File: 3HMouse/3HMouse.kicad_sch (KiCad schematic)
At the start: 78 parts, among them J1 USB_C_Receptacle, SW1 CherryMX, SW10 CherryMX, SW11 CherryMX, SW12 CherryMX, SW13 CherryMX, SW14 CherryMX, SW15 CherryMX, SW16 CherryMX, SW17 CherryMX, SW18 CherryMX, SW19 CherryMX, SW2 CherryMX, SW20 CherryMX, SW21 CherryMX, SW22 CherryMX, SW23 CherryMX, SW24 CherryMX, SW25 CherryMX, SW26 RotaryEncoder, SW27 RotaryEncoder, SW28 CherryMX, SW29 CherryMX, SW3 CherryMX, SW30 CherryMX, SW31 CherryMX, SW32 SW_Push, SW4 CherryMX, SW5 CherryMX, SW6 CherryMX, SW7 CherryMX, SW8 CherryMX, SW9 CherryMX, U1 AT90USB1286-A, Y1 16 MHz

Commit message: Updated Numbering for switches
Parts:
- renumbered SW28 to SW26, SW29 to SW27, SW30 to SW28, SW31 to SW29, SW26 to SW30, SW27 to SW31
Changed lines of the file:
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@@
   )
   (symbol (lib_id "CherryMX:CherryMX") (at 157.48 95.885 0) (unit 1)
-    (in_bom yes) (on_board yes) (fields_autoplaced)
-    (property "Reference" "SW31" (id 0) (at 157.48 88.265 0))
+    (in_bom yes) (on_board yes)
+    (property "Reference" "SW29" (id 0) (at 157.48 88.265 0))
     (property "Value" "CherryMX" (id 1) (at 157.48 90.805 0))
     (property "Footprint" "MX_Only:MXOnly-1U" (id 2) (at 157.48 95.25 0)
@@
   )
   (symbol (lib_id "CherryMX:CherryMX") (at 143.51 95.885 0) (unit 1)
-    (in_bom yes) (on_board yes) (fields_autoplaced)
-    (property "Reference" "SW29" (id 0) (at 143.51 88.265 0))
+    (in_bom yes) (on_board yes)
+    (property "Reference" "SW27" (id 0) (at 143.51 88.265 0))
     (property "Value" "CherryMX" (id 1) (at 143.51 90.805 0))
     (property "Footprint" "MX_Only:MXOnly-1U" (id 2) (at 143.51 95.25 0)
@@
   (symbol (lib_id "Device:RotaryEncoder") (at 133.35 34.29 0) (unit 1)
     (in_bom yes) (on_board yes) (fields_autoplaced)
-    (property "Reference" "SW26" (id 0) (at 139.7 33.0199 0)
+    (property "Reference" "SW30" (id 0) (at 139.7 33.0199 0)
       (effects (font (size 1.27 1.27)) (justify left))
     )
@@
   )
   (symbol (lib_id "CherryMX:CherryMX") (at 157.48 80.645 0) (unit 1)
-    (in_bom yes) (on_board yes) (fields_autoplaced)
-    (property "Reference" "SW30" (id 0) (at 157.48 73.025 0))
+    (in_bom yes) (on_board yes)
+    (property "Reference" "SW28" (id 0) (at 157.48 73.025 0))
     (property "Value" "CherryMX" (id 1) (at 157.48 75.565 0))
     (property "Footprint" "MX_Only:MXOnly-1U" (id 2) (at 157.48 80.01 0)
@@
   (symbol (lib_id "Device:RotaryEncoder") (at 133.35 46.355 0) (unit 1)
     (in_bom yes) (on_board yes) (fields_autoplaced)
-    (property "Reference" "SW27" (id 0) (at 139.7 45.0849 0)
+    (property "Reference" "SW31" (id 0) (at 139.7 45.0849 0)
       (effects (font (size 1.27 1.27)) (justify left))
     )
@@
   )
   (symbol (lib_id "CherryMX:CherryMX") (at 143.51 80.645 0) (unit 1)
-    (in_bom yes) (on_board yes) (fields_autoplaced)
-    (property "Reference" "SW28" (id 0) (at 143.51 73.025 0))
+    (in_bom yes) (on_board yes)
+    (property "Reference" "SW26" (id 0) (at 143.51 73.025 0))
     (property "Value" "CherryMX" (id 1) (at 143.51 75.565 0))
     (property "Footprint" "MX_Only:MXOnly-1U" (id 2) (at 143.51 80.01 0)
@@
       (reference "SW25") (unit 1) (value "CherryMX") (footprint "MX_Only:MXOnly-1U")
     )
+    (path "/e0216e84-2ce2-4d70-a198-14f8e2650f46"
+      (reference "SW26") (unit 1) (value "CherryMX") (footprint "MX_Only:MXOnly-1U")
+    )
+    (path "/0fa31cb8-7672-48e3-a3df-ba70a523e3f0"
+      (reference "SW27") (unit 1) (value "CherryMX") (footprint "MX_Only:MXOnly-1U")
+    )
+    (path "/81b3182e-bef8-43da-b30b-949829e17b92"
+      (reference "SW28") (unit 1) (value "CherryMX") (footprint "MX_Only:MXOnly-1U")
+    )
+    (path "/03450b8f-fc4d-434e-bd58-3aa679557c4b"
+      (reference "SW29") (unit 1) (value "CherryMX") (footprint "MX_Only:MXOnly-1U")
+    )
     (path "/7084012f-9f53-49a4-9f6c-0fc49f2f085e"
-      (reference "SW26") (unit 1) (value "RotaryEncoder") (footprint "Keebio-Parts:RotaryEncoder_EC11")
+      (reference "SW30") (unit 1) (value "RotaryEncoder") (footprint "Keebio-Parts:RotaryEncoder_EC11")
     )
     (path "/85fe6307-0285-4bd4-aaf9-c64a8b5619b6"
-      (reference "SW27") (unit 1) (value "RotaryEncoder") (footprint "Keebio-Parts:RotaryEncoder_EC11")
-    )
-    (path "/e0216e84-2ce2-4d70-a198-14f8e2650f46"
-      (reference "SW28") (unit 1) (value "CherryMX") (footprint "MX_Only:MXOnly-1U")
-    )
-    (path "/0fa31cb8-7672-48e3-a3df-ba70a523e3f0"
-      (reference "SW29") (unit 1) (value "CherryMX") (footprint "MX_Only:MXOnly-1U")
-    )
-    (path "/81b3182e-bef8-43da-b30b-949829e17b92"
-      (reference "SW30") (unit 1) (value "CherryMX") (footprint "MX_Only:MXOnly-1U")
-    )
-    (path "/03450b8f-fc4d-434e-bd58-3aa679557c4b"
-      (reference "SW31") (unit 1) (value "CherryMX") (footprint "MX_Only:MXOnly-1U")
+      (reference "SW31") (unit 1) (value "RotaryEncoder") (footprint "Keebio-Parts:RotaryEncoder_EC11")
     )
     (path "/f38537ef-e8e3-4868-a9d5-b9b5e50ace08"

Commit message: v0.1.0
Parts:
- added Brd1: SSD1306, SSD1306:128x64OLED, symbol SSD1306-128x64_OLED:SSD1306
- added C3: 0.1uF, Capacitor_SMD:C_0805_2012Metric, symbol Device:C_Small
- J1: footprint Connector_USB:USB_C_Receptacle_GCT_USB4085 -> Connector_USB:USB_C_Receptacle_Amphenol_12401548E4-2A
- renumbered C3 to C8
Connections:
- net +5V: now also Brd1.2 (VCC), C3.2
- net COL0: now also U1.12 (PB2)
- net COL1: now also U1.13 (PB3)
- net COL2: now also U1.14 (PB4)
- net COL3: now also U1.15 (PB5)
- net COL4: now also U1.16 (PB6)
- net COL5: now also U1.17 (PB7)
- net COL6: now also U1.33 (PE0)
- net COL7: now also U1.34 (PE1)
- net COL8: now also U1.35 (PC0)
- net COL9: now also U1.36 (PC1)
- net GND: now also Brd1.1 (GND), C3.1
- net ROW0: now also U1.37 (PC2)
- net ROW1: now also U1.38 (PC3)
- net ROW2: now also U1.39 (PC4)
- net ROW3: now also U1.40 (PC5)
- net ROW4: now also U1.41 (PC6)
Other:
- moved on the sheet: C4

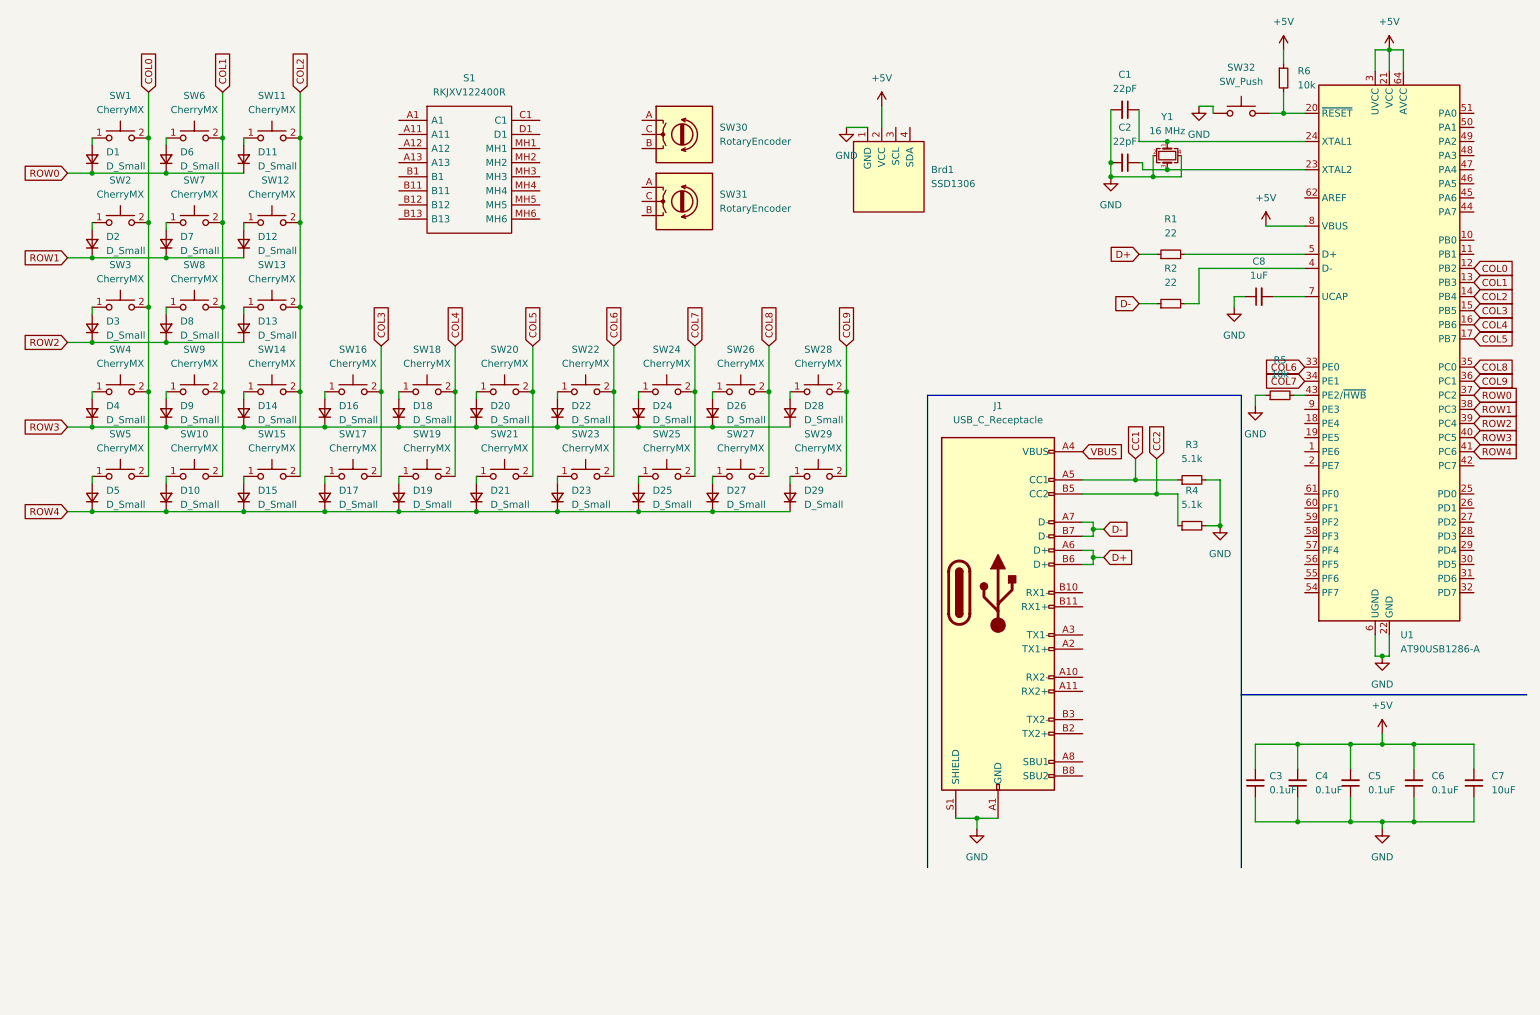
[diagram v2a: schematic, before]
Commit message: Added ESD Protection and wired Joystick and Encoders
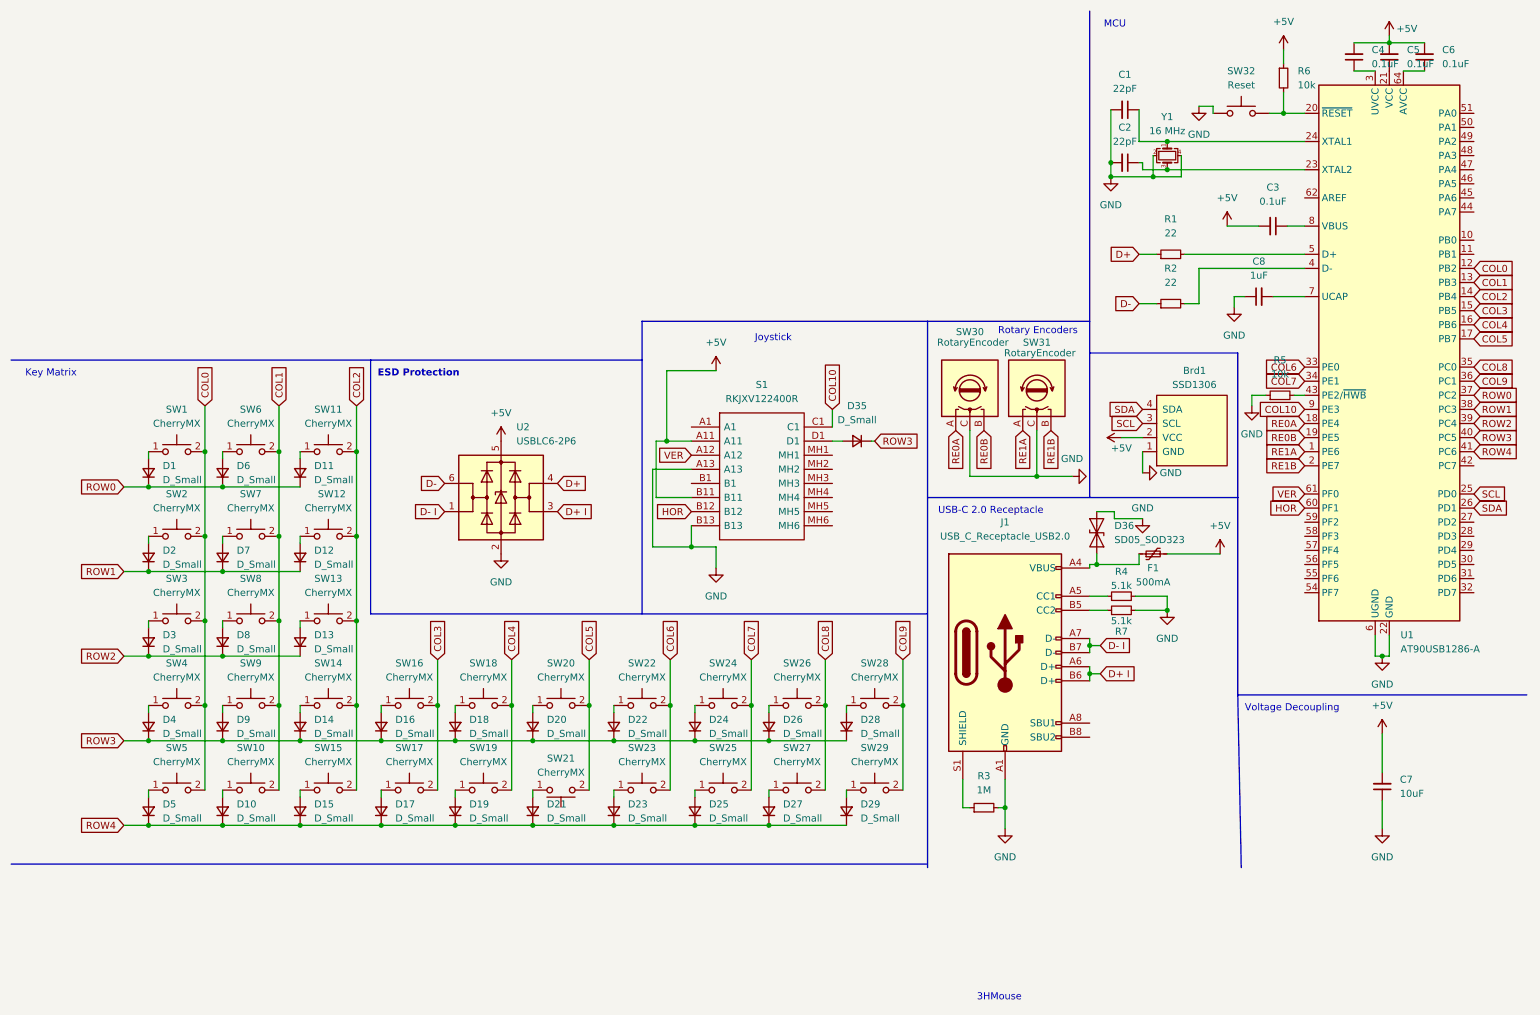
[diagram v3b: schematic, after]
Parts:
- removed J1: USB_C_Receptacle, Connector_USB:USB_C_Receptacle_Amphenol_12401548E4-2A, symbol Connector:USB_C_Receptacle
- added D35: D_Small, Diode_SMD:D_SOD-123, symbol Device:D_Small
- added D36: SD05_SOD323, Diode_SMD:D_SOD-323, symbol Diode:SD05_SOD323
- added F1: 500mA, Fuse:Fuse_1206_3216Metric, symbol Device:Polyfuse_Small
- added J1: USB_C_Receptacle_USB2.0, Connector_USB:USB_C_Receptacle_GCT_USB4085, symbol Connector:USB_C_Receptacle_USB2.0
- added R7: 5.1k, Resistor_SMD:R_0805_2012Metric, symbol Device:R_Small
- added U2: USBLC6-2P6, Package_TO_SOT_SMD:SOT-666, symbol Power_Protection:USBLC6-2P6
- R3: value 5.1k -> 1M
- SW32: value SW_Push -> Reset
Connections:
- net +5V: now also S1.A11, S1.B11, F1.2, U2.5 (VBUS); no longer U1.21 (VCC), U1.3 (UVCC), U1.52 (VCC), U1.64 (AVCC), U1.8 (VBUS)
- net D+: now also U2.4 (I/O2)
- net D-: now also U2.6 (I/O1)
- net GND: now also S1.A13, S1.B13, SW30.C, SW31.C, D36.2 (A2), J1.A1 (GND), J1.A12 (GND), J1.B1 (GND), J1.B12 (GND), R7.2, U2.2 (GND); no longer C3.1, C4.1, C5.1, C6.1
- net ROW3: now also D35.1 (K)
- net RE0A: now reaches SW30.A
- net RE0A: now also U1.18 (PE4)
- net RE0B: now reaches SW30.B
- net RE0B: now also U1.19 (PE5)
- net RE1A: now reaches U1.1 (PE6)
- net RE1A: now also SW31.A
- net RE1B: now reaches U1.2 (PE7)
- net RE1B: now also SW31.B
- net SCL: now reaches U1.25 (PD0)
- net SCL: now also Brd1.3 (SCL)
- net SDA: now reaches U1.26 (PD1)
- net SDA: now also Brd1.4 (SDA)
- net HOR: now reaches U1.60 (PF1)
- net HOR: now also S1.B12
- net VER: now reaches U1.61 (PF0)
- net VER: now also S1.A12
- net COL10: now reaches U1.9 (PE3)
- net COL10: now also S1.C1
- net at S1.D1: now also D35.2 (A)
- net CC1: no longer names the net of R3.1
- net CC1: now also J1.S1 (SHIELD)
- net CC2: no longer names the net of R4.1
- net CC2: now also J1.A5 (CC1)
- new net: C6.1, U1.64 (AVCC)
- new net: C4.1, U1.3 (UVCC)
- new net: D36.1 (A1), F1.1, J1.A4 (VBUS), J1.A9 (VBUS), J1.B4 (VBUS), J1.B9 (VBUS)
- new net: C5.1, U1.21 (VCC), U1.52 (VCC)
- new net: C3.1, U1.8 (VBUS)
- new net: J1.B5 (CC2), R7.1
- new net D+ I: J1.A6 (D+), J1.B6 (D+), U2.3 (I/O2)
- new net D- I: J1.A7 (D-), J1.B7 (D-), U2.1 (I/O1)
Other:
- note added: "3HMouse"
- note added: "ESD Protection"
- note added: "Joystick"
- note added: "Key Matrix"
- note added: "MCU"
- note added: "Rotary Encoders"
- note added: "USB-C 2.0 Receptacle"
- note added: "Voltage Decoupling"
- moved on the sheet: Brd1, C7, D1, D10, D11, D12, D13, D14, D15, D16, D17, D18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

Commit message: Added NC to Schematic
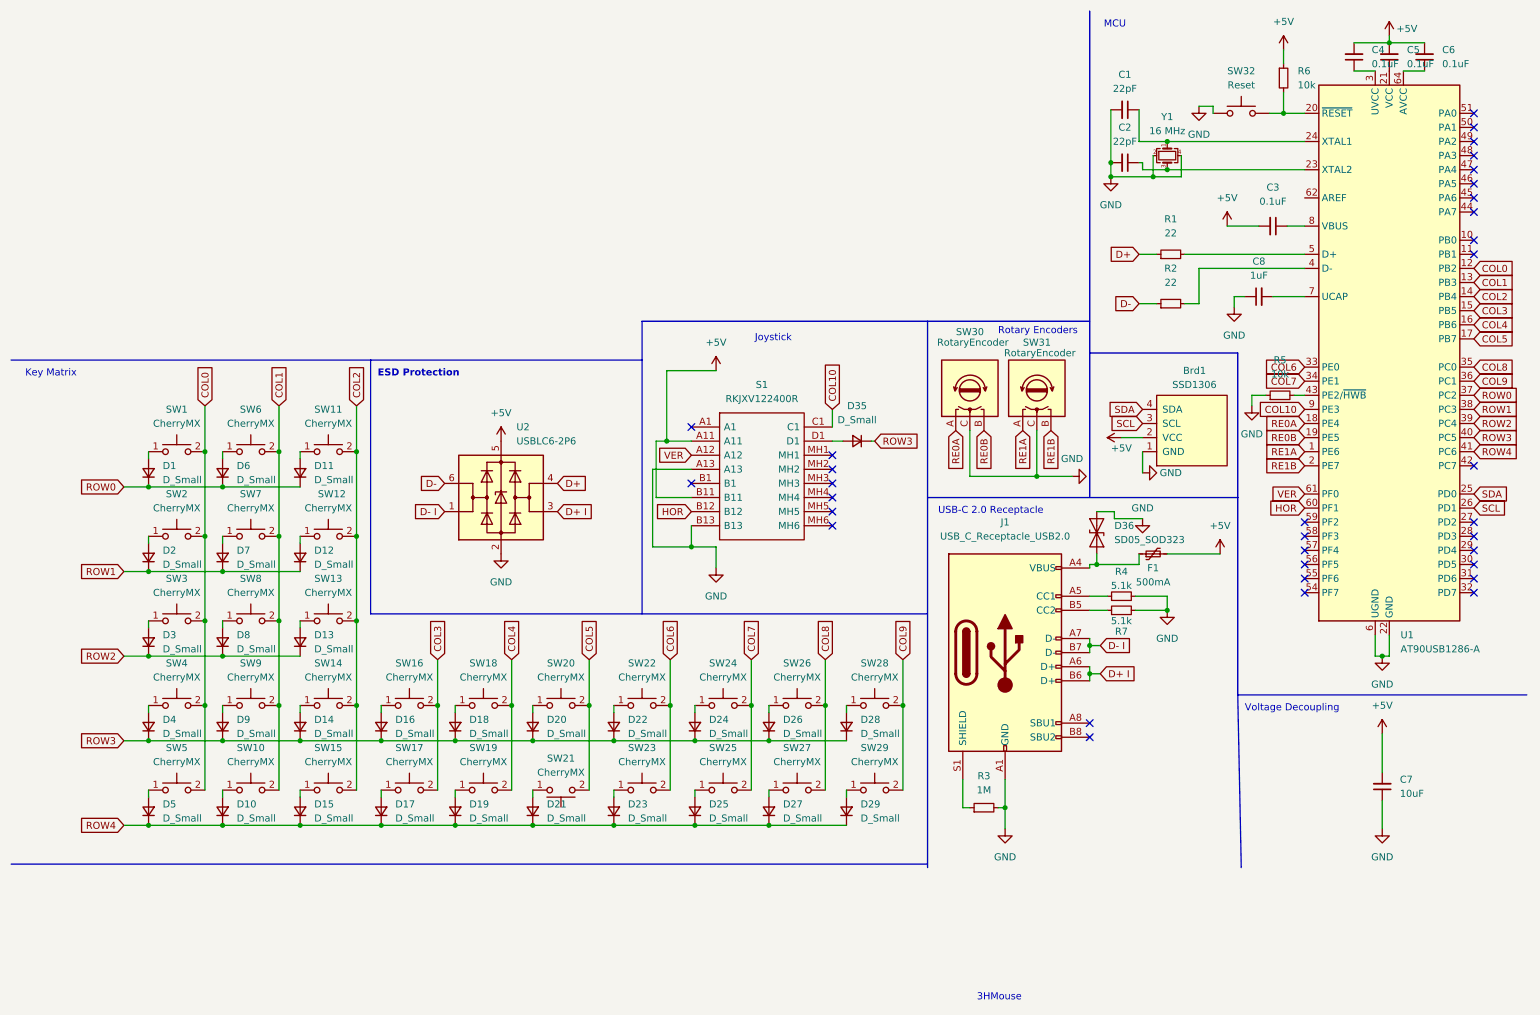
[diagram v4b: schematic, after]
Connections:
- net SCL: now also U1.26 (PD1); no longer U1.25 (PD0)
- net SDA: now also U1.25 (PD0); no longer U1.26 (PD1)
- no-connect marks 0 -> 33
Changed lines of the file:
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@@
   (junction (at 46.99 91.44) (diameter 0) (color 0 0 0 0)
   )
+  (no_connect (at 275.59 30.48))
+  (no_connect (at 275.59 33.02))
+  (no_connect (at 275.59 55.88))
+  (no_connect (at 275.59 53.34))
+  (no_connect (at 275.59 48.26))
+  (no_connect (at 275.59 45.72))
+  (no_connect (at 275.59 43.18))
+  (no_connect (at 275.59 40.64))
+  (no_connect (at 275.59 38.1))
+  (no_connect (at 275.59 35.56))
+  (no_connect (at 206.375 140.335))
+  (no_connect (at 206.375 142.875))
+  (no_connect (at 275.59 104.14))
+  (no_connect (at 275.59 93.98))
+  (no_connect (at 245.11 111.76))
+  (no_connect (at 245.11 114.3))
+  (no_connect (at 245.11 116.84))
+  (no_connect (at 245.11 104.14))
+  (no_connect (at 245.11 106.68))
+  (no_connect (at 245.11 109.22))
+  (no_connect (at 275.59 106.68))
+  (no_connect (at 275.59 109.22))
+  (no_connect (at 275.59 111.76))
+  (no_connect (at 275.59 114.3))
+  (no_connect (at 275.59 116.84))
+  (no_connect (at 160.02 104.775))
+  (no_connect (at 134.62 97.155))
+  (no_connect (at 134.62 86.995))
+  (no_connect (at 160.02 92.075))
+  (no_connect (at 160.02 94.615))
+  (no_connect (at 160.02 97.155))
+  (no_connect (at 160.02 99.695))
+  (no_connect (at 160.02 102.235))
   (wire (pts (xy 127.635 108.585) (xy 134.62 108.585))
     (stroke (width 0) (type default) (color 0 0 0 0))
@@
     (effects (font (size 1.27 1.27)) (justify left bottom))
   )
+  (global_label "SDA" (shape input) (at 275.59 99.06 0) (fields_autoplaced)
+    (effects (font (size 1.27 1.27)) (justify left))
+    (property "Intersheet References" "${INTERSHEET_REFS}" (id 0) (at 281.5712 98.9806 0)
+      (effects (font (size 1.27 1.27)) (justify left) hide)
+    )
+  )
   (global_label "RE1A" (shape input) (at 245.11 91.44 180) (fields_autoplaced)
     (effects (font (size 1.27 1.27)) (justify right))
@@
     )
   )
-  (global_label "SCL" (shape input) (at 275.59 99.06 0) (fields_autoplaced)
-    (effects (font (size 1.27 1.27)) (justify left))
-    (property "Intersheet References" "${INTERSHEET_REFS}" (id 0) (at 281.5107 98.9806 0)
-      (effects (font (size 1.27 1.27)) (justify left) hide)
-    )
-  )
   (global_label "COL1" (shape input) (at 275.59 60.96 0) (fields_autoplaced)
     (effects (font (size 1.27 1.27)) (justify left))
@@
     )
   )
+  (global_label "SCL" (shape input) (at 275.59 101.6 0) (fields_autoplaced)
+    (effects (font (size 1.27 1.27)) (justify left))
+    (property "Intersheet References" "${INTERSHEET_REFS}" (id 0) (at 281.5107 101.5206 0)
+      (effects (font (size 1.27 1.27)) (justify left) hide)
+    )
+  )
   (global_label "COL6" (shape input) (at 245.11 76.2 180) (fields_autoplaced)
     (effects (font (size 1.27 1.27)) (justify right))
@@
     )
   )
-  (global_label "SDA" (shape input) (at 275.59 101.6 0) (fields_autoplaced)
-    (effects (font (size 1.27 1.27)) (justify left))
-    (property "Intersheet References" "${INTERSHEET_REFS}" (id 0) (at 281.5712 101.5206 0)
-      (effects (font (size 1.27 1.27)) (justify left) hide)
-    )
-  )

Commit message: Finished Initial Routing
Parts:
- removed U2: USBLC6-2P6, Package_TO_SOT_SMD:SOT-666, symbol Power_Protection:USBLC6-2P6
- added U2: USBLC6-2SC6, Package_TO_SOT_SMD:SOT-23-6, symbol Power_Protection:USBLC6-2SC6
- SW1, SW11, SW12, SW13, SW14, SW15, SW16, SW17, SW18, SW19, SW2, SW20, SW21, SW22, SW23, SW24, SW25, SW26, SW27, SW28, SW29, SW3, SW6, SW7, SW8, SW9: footprint MX_Only:MXOnly-1U -> MX_Only:MXOnly-1U-NoLED
- SW10, SW5: footprint MX_Only:MXOnly-1U -> MX_Only:MXOnly-1.25U-NoLED
- SW4: footprint MX_Only:MXOnly-1U -> MX_Only:MXOnly-1.5U-NoLED
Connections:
- net +5V: now also U2.5 (VBUS)
- net D+: now also U2.4 (I/O2)
- net D+ I: now also U2.3 (I/O2)
- net D-: now also U2.6 (I/O1)
- net D- I: now also U2.1 (I/O1)
- net GND: now also U2.2 (GND)
- net HOR: now also U1.61 (PF0); no longer U1.60 (PF1)
- net RE0A: now also U1.46 (PA5); no longer U1.18 (PE4)
- net RE0B: now also U1.45 (PA6); no longer U1.19 (PE5)
- net RE1A: now also U1.48 (PA3); no longer U1.1 (PE6)
- net RE1B: now also U1.47 (PA4); no longer U1.2 (PE7)
- net ROW0: now also U1.39 (PC4); no longer U1.37 (PC2)
- net ROW2: now also U1.37 (PC2); no longer U1.39 (PC4)
- net VER: now also U1.60 (PF1); no longer U1.61 (PF0)
- no-connect marks 33 -> 34
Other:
- note added: "ERC Power"
